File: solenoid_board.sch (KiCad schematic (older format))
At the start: 38 parts, among them J2 MCU_LEFT_LEGS, J3 MCU_RIGHT_LEGS

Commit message: Changed the resistor footprints, and sourced new resistors in the BOM. Need to route the wires.
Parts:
- R10, R100, R101, R102, R103, R104, R105, R11: footprint Resistor_SMD:R_2010_5025Metric_Pad1.52x2.65mm_HandSolder -> Resistor_THT:R_Axial_DIN0309_L9.0mm_D3.2mm_P20.32mm_Horizontal
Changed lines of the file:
@@
 F 0 "R100" V 5200 1900 50  0000 C CNN
 F 1 "100" V 5400 1900 50  0000 C CNN
-F 2 "Resistor_SMD:R_2010_5025Metric_Pad1.52x2.65mm_HandSolder" V 5230 1900 50  0001 C CNN
+F 2 "Resistor_THT:R_Axial_DIN0309_L9.0mm_D3.2mm_P20.32mm_Horizontal" V 5230 1900 50  0001 C CNN
 F 3 "~" H 5300 1900 50  0001 C CNN
 	1    5300 1900
@@
 F 0 "R101" V 5950 2400 50  0000 C CNN
 F 1 "100" V 6150 2400 50  0000 C CNN
-F 2 "Resistor_SMD:R_2010_5025Metric_Pad1.52x2.65mm_HandSolder" V 5980 2400 50  0001 C CNN
+F 2 "Resistor_THT:R_Axial_DIN0309_L9.0mm_D3.2mm_P20.32mm_Horizontal" V 5980 2400 50  0001 C CNN
 F 3 "~" H 6050 2400 50  0001 C CNN
 	1    6050 2400
@@
 F 0 "R102" V 6700 2900 50  0000 C CNN
 F 1 "100" V 6900 2900 50  0000 C CNN
-F 2 "Resistor_SMD:R_2010_5025Metric_Pad1.52x2.65mm_HandSolder" V 6730 2900 50  0001 C CNN
+F 2 "Resistor_THT:R_Axial_DIN0309_L9.0mm_D3.2mm_P20.32mm_Horizontal" V 6730 2900 50  0001 C CNN
 F 3 "~" H 6800 2900 50  0001 C CNN
 	1    6800 2900
@@
 F 0 "R103" V 7450 3400 50  0000 C CNN
 F 1 "100" V 7650 3400 50  0000 C CNN
-F 2 "Resistor_SMD:R_2010_5025Metric_Pad1.52x2.65mm_HandSolder" V 7480 3400 50  0001 C CNN
+F 2 "Resistor_THT:R_Axial_DIN0309_L9.0mm_D3.2mm_P20.32mm_Horizontal" V 7480 3400 50  0001 C CNN
 F 3 "~" H 7550 3400 50  0001 C CNN
 	1    7550 3400
@@
 F 0 "R104" V 8200 3900 50  0000 C CNN
 F 1 "100" V 8400 3900 50  0000 C CNN
-F 2 "Resistor_SMD:R_2010_5025Metric_Pad1.52x2.65mm_HandSolder" V 8230 3900 50  0001 C CNN
+F 2 "Resistor_THT:R_Axial_DIN0309_L9.0mm_D3.2mm_P20.32mm_Horizontal" V 8230 3900 50  0001 C CNN
 F 3 "~" H 8300 3900 50  0001 C CNN
 	1    8300 3900
@@
 F 0 "R105" V 8950 4400 50  0000 C CNN
 F 1 "100" V 9150 4400 50  0000 C CNN
-F 2 "Resistor_SMD:R_2010_5025Metric_Pad1.52x2.65mm_HandSolder" V 8980 4400 50  0001 C CNN
+F 2 "Resistor_THT:R_Axial_DIN0309_L9.0mm_D3.2mm_P20.32mm_Horizontal" V 8980 4400 50  0001 C CNN
 F 3 "~" H 9050 4400 50  0001 C CNN
 	1    9050 4400
@@
 F 0 "R11" V 2800 3600 50  0000 C CNN
 F 1 "10" V 2600 3600 50  0001 C CNN
-F 2 "Resistor_SMD:R_2010_5025Metric_Pad1.52x2.65mm_HandSolder" V 2630 3600 50  0001 C CNN
+F 2 "Resistor_THT:R_Axial_DIN0309_L9.0mm_D3.2mm_P20.32mm_Horizontal" V 2630 3600 50  0001 C CNN
 F 3 "~" H 2700 3600 50  0001 C CNN
 	1    2700 3600
@@
 F 0 "R10" V 2600 3350 50  0000 C CNN
 F 1 "10" V 2584 3350 50  0001 C CNN
-F 2 "Resistor_SMD:R_2010_5025Metric_Pad1.52x2.65mm_HandSolder" V 2630 3350 50  0001 C CNN
+F 2 "Resistor_THT:R_Axial_DIN0309_L9.0mm_D3.2mm_P20.32mm_Horizontal" V 2630 3350 50  0001 C CNN
 F 3 "~" H 2700 3350 50  0001 C CNN
 	1    2700 3350

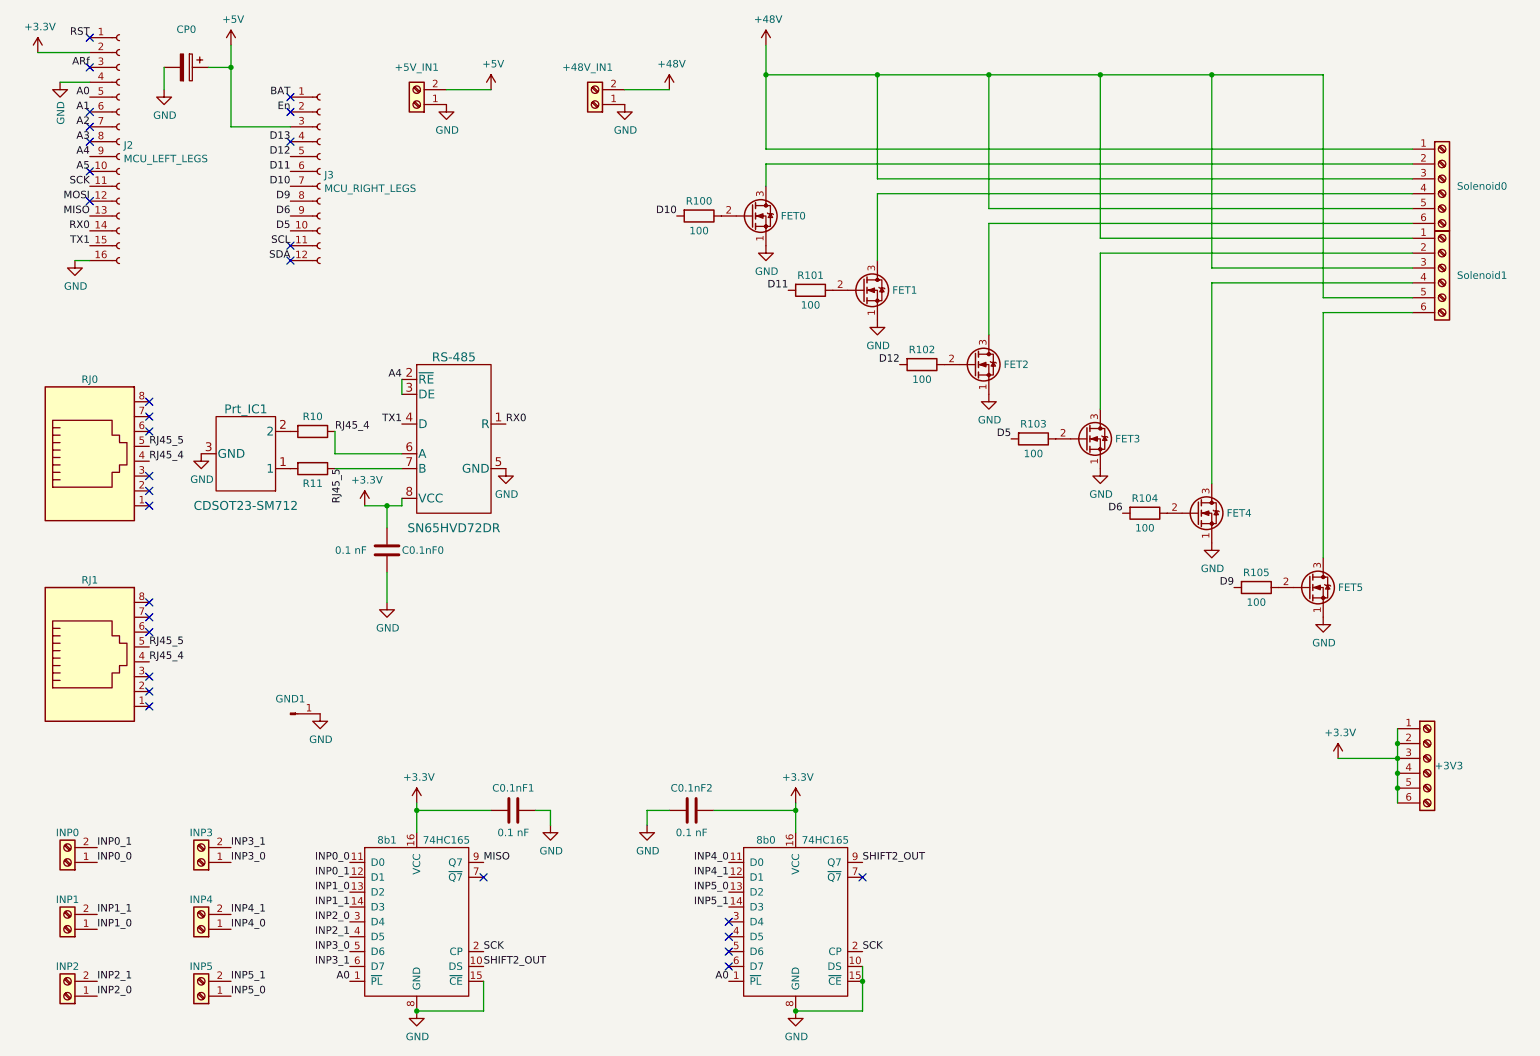
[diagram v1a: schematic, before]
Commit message: Swapped out screw terminals for pin headers.
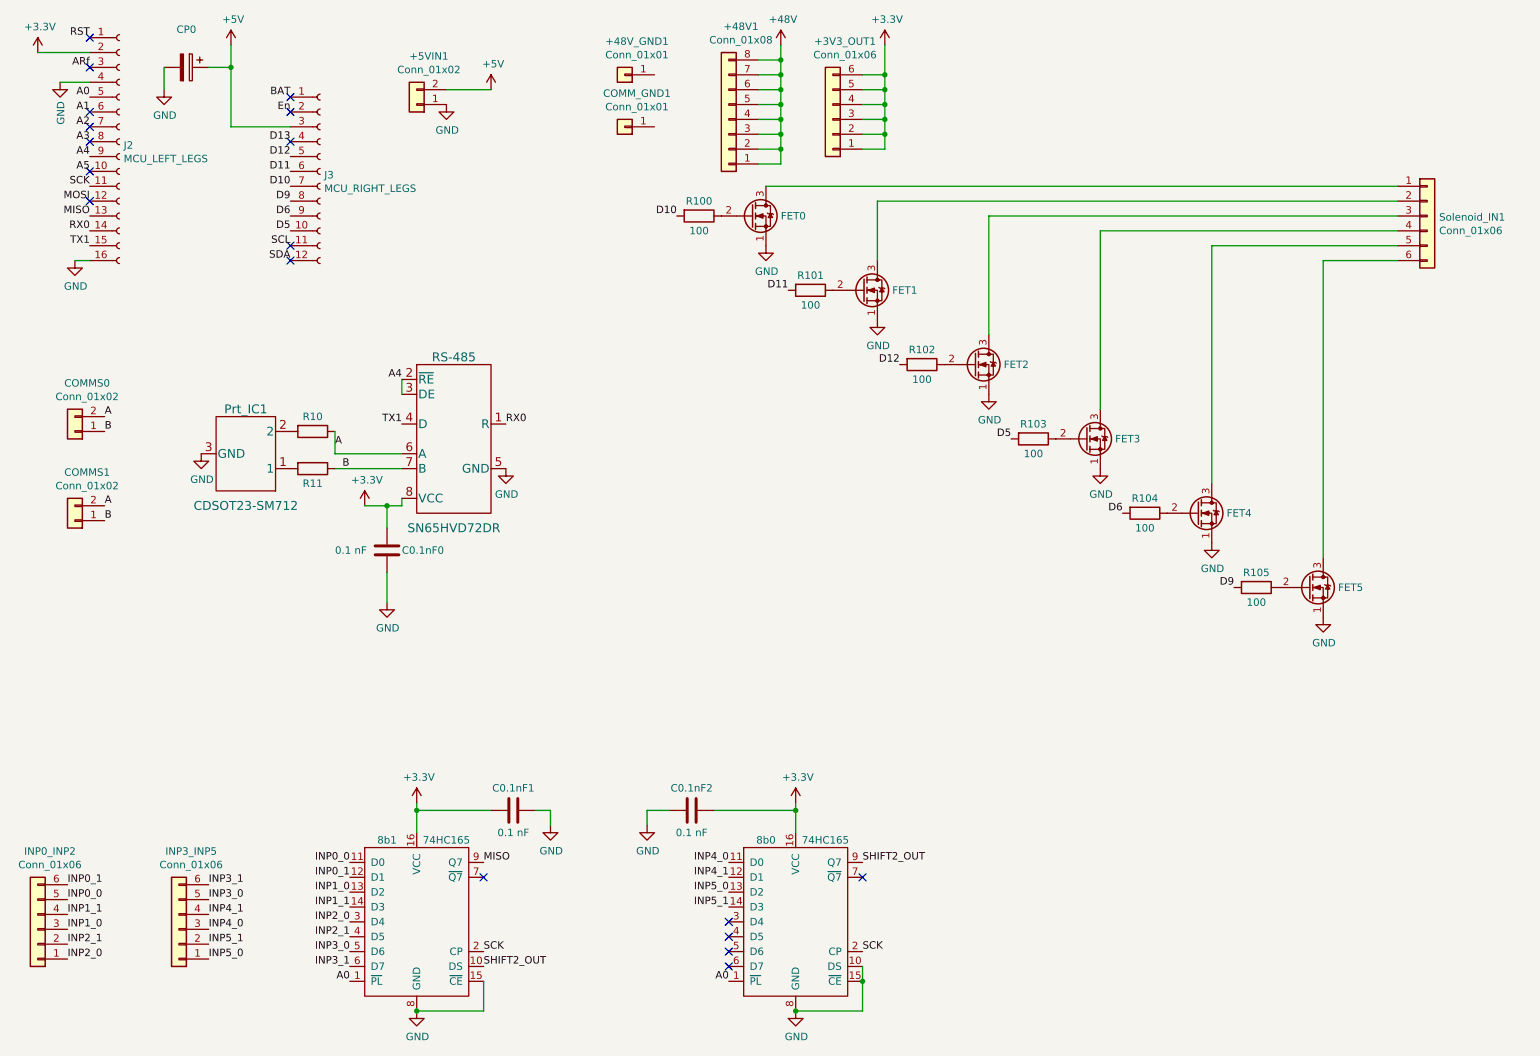
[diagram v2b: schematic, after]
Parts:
- removed +3V3, Solenoid0, Solenoid1: Screw_Terminal_01x06, TerminalBlock:TerminalBlock_bornier-6_P5.08mm, symbol Connector:Screw_Terminal_01x06
- removed +48V_IN1: Solenoid_PWR_Supply, TerminalBlock:TerminalBlock_bornier-2_P5.08mm, symbol Connector:Screw_Terminal_01x02
- removed +5V_IN1: MCU_PWR_Supply, TerminalBlock:TerminalBlock_bornier-2_P5.08mm, symbol Connector:Screw_Terminal_01x02
- removed GND1: Conn_01x01_Male, Connector_PinHeader_2.54mm:PinHeader_1x01_P2.54mm_Vertical, symbol Connector:Conn_01x01_Male
- removed INP0, INP1, INP2, INP3, INP4, INP5: Screw_Terminal_01x02, TerminalBlock:TerminalBlock_bornier-2_P5.08mm, symbol Connector:Screw_Terminal_01x02
- removed RJ0, RJ1: RJ45, Connector_RJ:RJ45_Amphenol_54602-x08_Horizontal, symbol Connector:RJ45
- added +3V3_OUT1, INP0_INP2, INP3_INP5, Solenoid_IN1: Conn_01x06, Connector_PinHeader_2.54mm:PinHeader_1x06_P2.54mm_Vertical, symbol Connector_Generic:Conn_01x06
- added +48V1: Conn_01x08, Connector_PinHeader_2.54mm:PinHeader_1x08_P2.54mm_Vertical, symbol Connector_Generic:Conn_01x08
- added +48V_GND1, COMM_GND1: Conn_01x01, Connector_PinHeader_2.54mm:PinHeader_1x01_P2.54mm_Vertical, symbol Connector_Generic:Conn_01x01
- added +5VIN1, COMMS0, COMMS1: Conn_01x02, Connector_PinHeader_2.54mm:PinHeader_1x02_P2.54mm_Vertical, symbol Connector_Generic:Conn_01x02
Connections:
- net +3V3: now also +3V3_OUT1.1 (Pin_1), +3V3_OUT1.2 (Pin_2), +3V3_OUT1.3 (Pin_3), +3V3_OUT1.4 (Pin_4), +3V3_OUT1.5 (Pin_5), +3V3_OUT1.6 (Pin_6)
- net +48V: now also +48V1.1 (Pin_1), +48V1.2 (Pin_2), +48V1.3 (Pin_3), +48V1.4 (Pin_4), +48V1.5 (Pin_5), +48V1.6 (Pin_6), +48V1.7 (Pin_7), +48V1.8 (Pin_8)
- net +5V: now also +5VIN1.2 (Pin_2)
- net GND: now also +5VIN1.1 (Pin_1)
- net INP0_0: now also INP0_INP2.5 (Pin_5)
- net INP0_1: now also INP0_INP2.6 (Pin_6)
- net INP1_0: now also INP0_INP2.3 (Pin_3)
- net INP1_1: now also INP0_INP2.4 (Pin_4)
- net INP2_0: now also INP0_INP2.1 (Pin_1)
- net INP2_1: now also INP0_INP2.2 (Pin_2)
- net INP3_0: now also INP3_INP5.5 (Pin_5)
- net INP3_1: now also INP3_INP5.6 (Pin_6)
- net INP4_0: now also INP3_INP5.3 (Pin_3)
- net INP4_1: now also INP3_INP5.4 (Pin_4)
- net INP5_0: now also INP3_INP5.1 (Pin_1)
- net INP5_1: now also INP3_INP5.2 (Pin_2)
- net at FET0.3 (D): now also Solenoid_IN1.1 (Pin_1)
- net at FET1.3 (D): now also Solenoid_IN1.2 (Pin_2)
- net at FET2.3 (D): now also Solenoid_IN1.3 (Pin_3)
- net at FET3.3 (D): now also Solenoid_IN1.4 (Pin_4)
- net at FET4.3 (D): now also Solenoid_IN1.5 (Pin_5)
- net at FET5.3 (D): now also Solenoid_IN1.6 (Pin_6)
- net RJ45_4 renamed A
- net A: now also COMMS0.2 (Pin_2), COMMS1.2 (Pin_2)
- net RJ45_5 renamed B
- net B: now also COMMS0.1 (Pin_1), COMMS1.1 (Pin_1)
- no-connect marks 30 -> 18

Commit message: Changed Resistor Footprint to save space. Need to rename symbolic connections to allow for better routing.
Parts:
- R10, R100, R101, R102, R103, R104, R105, R11: footprint Resistor_THT:R_Axial_DIN0309_L9.0mm_D3.2mm_P20.32mm_Horizontal -> Resistor_THT:R_Axial_DIN0204_L3.6mm_D1.6mm_P5.08mm_Vertical
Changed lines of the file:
@@
 F 0 "R100" V 5200 1900 50  0000 C CNN
 F 1 "100" V 5400 1900 50  0000 C CNN
-F 2 "Resistor_THT:R_Axial_DIN0309_L9.0mm_D3.2mm_P20.32mm_Horizontal" V 5230 1900 50  0001 C CNN
+F 2 "Resistor_THT:R_Axial_DIN0204_L3.6mm_D1.6mm_P5.08mm_Vertical" V 5230 1900 50  0001 C CNN
 F 3 "~" H 5300 1900 50  0001 C CNN
 	1    5300 1900
@@
 F 0 "R101" V 5950 2400 50  0000 C CNN
 F 1 "100" V 6150 2400 50  0000 C CNN
-F 2 "Resistor_THT:R_Axial_DIN0309_L9.0mm_D3.2mm_P20.32mm_Horizontal" V 5980 2400 50  0001 C CNN
+F 2 "Resistor_THT:R_Axial_DIN0204_L3.6mm_D1.6mm_P5.08mm_Vertical" V 5980 2400 50  0001 C CNN
 F 3 "~" H 6050 2400 50  0001 C CNN
 	1    6050 2400
@@
 F 0 "R102" V 6700 2900 50  0000 C CNN
 F 1 "100" V 6900 2900 50  0000 C CNN
-F 2 "Resistor_THT:R_Axial_DIN0309_L9.0mm_D3.2mm_P20.32mm_Horizontal" V 6730 2900 50  0001 C CNN
+F 2 "Resistor_THT:R_Axial_DIN0204_L3.6mm_D1.6mm_P5.08mm_Vertical" V 6730 2900 50  0001 C CNN
 F 3 "~" H 6800 2900 50  0001 C CNN
 	1    6800 2900
@@
 F 0 "R103" V 7450 3400 50  0000 C CNN
 F 1 "100" V 7650 3400 50  0000 C CNN
-F 2 "Resistor_THT:R_Axial_DIN0309_L9.0mm_D3.2mm_P20.32mm_Horizontal" V 7480 3400 50  0001 C CNN
+F 2 "Resistor_THT:R_Axial_DIN0204_L3.6mm_D1.6mm_P5.08mm_Vertical" V 7480 3400 50  0001 C CNN
 F 3 "~" H 7550 3400 50  0001 C CNN
 	1    7550 3400
@@
 F 0 "R104" V 8200 3900 50  0000 C CNN
 F 1 "100" V 8400 3900 50  0000 C CNN
-F 2 "Resistor_THT:R_Axial_DIN0309_L9.0mm_D3.2mm_P20.32mm_Horizontal" V 8230 3900 50  0001 C CNN
+F 2 "Resistor_THT:R_Axial_DIN0204_L3.6mm_D1.6mm_P5.08mm_Vertical" V 8230 3900 50  0001 C CNN
 F 3 "~" H 8300 3900 50  0001 C CNN
 	1    8300 3900
@@
 F 0 "R105" V 8950 4400 50  0000 C CNN
 F 1 "100" V 9150 4400 50  0000 C CNN
-F 2 "Resistor_THT:R_Axial_DIN0309_L9.0mm_D3.2mm_P20.32mm_Horizontal" V 8980 4400 50  0001 C CNN
+F 2 "Resistor_THT:R_Axial_DIN0204_L3.6mm_D1.6mm_P5.08mm_Vertical" V 8980 4400 50  0001 C CNN
 F 3 "~" H 9050 4400 50  0001 C CNN
 	1    9050 4400
@@
 F 0 "R11" V 2800 3600 50  0000 C CNN
 F 1 "10" V 2600 3600 50  0001 C CNN
-F 2 "Resistor_THT:R_Axial_DIN0309_L9.0mm_D3.2mm_P20.32mm_Horizontal" V 2630 3600 50  0001 C CNN
+F 2 "Resistor_THT:R_Axial_DIN0204_L3.6mm_D1.6mm_P5.08mm_Vertical" V 2630 3600 50  0001 C CNN
 F 3 "~" H 2700 3600 50  0001 C CNN
 	1    2700 3600
@@
 F 0 "R10" V 2600 3350 50  0000 C CNN
 F 1 "10" V 2584 3350 50  0001 C CNN
-F 2 "Resistor_THT:R_Axial_DIN0309_L9.0mm_D3.2mm_P20.32mm_Horizontal" V 2630 3350 50  0001 C CNN
+F 2 "Resistor_THT:R_Axial_DIN0204_L3.6mm_D1.6mm_P5.08mm_Vertical" V 2630 3350 50  0001 C CNN
 F 3 "~" H 2700 3350 50  0001 C CNN
 	1    2700 3350
